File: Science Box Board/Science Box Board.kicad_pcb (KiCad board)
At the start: 2 copper layers, 124.5 x 81.3 mm, 43 parts, among them U1 Molex_SL-2, U10 LB1930MC, U11 Molex_SL-10, U12 Molex_SL_2, U13 Molex_SL_5, U2 Molex_SL-2, U3 5V OKI, U4 OPA320, U5 OPA320, U6 5V OKI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

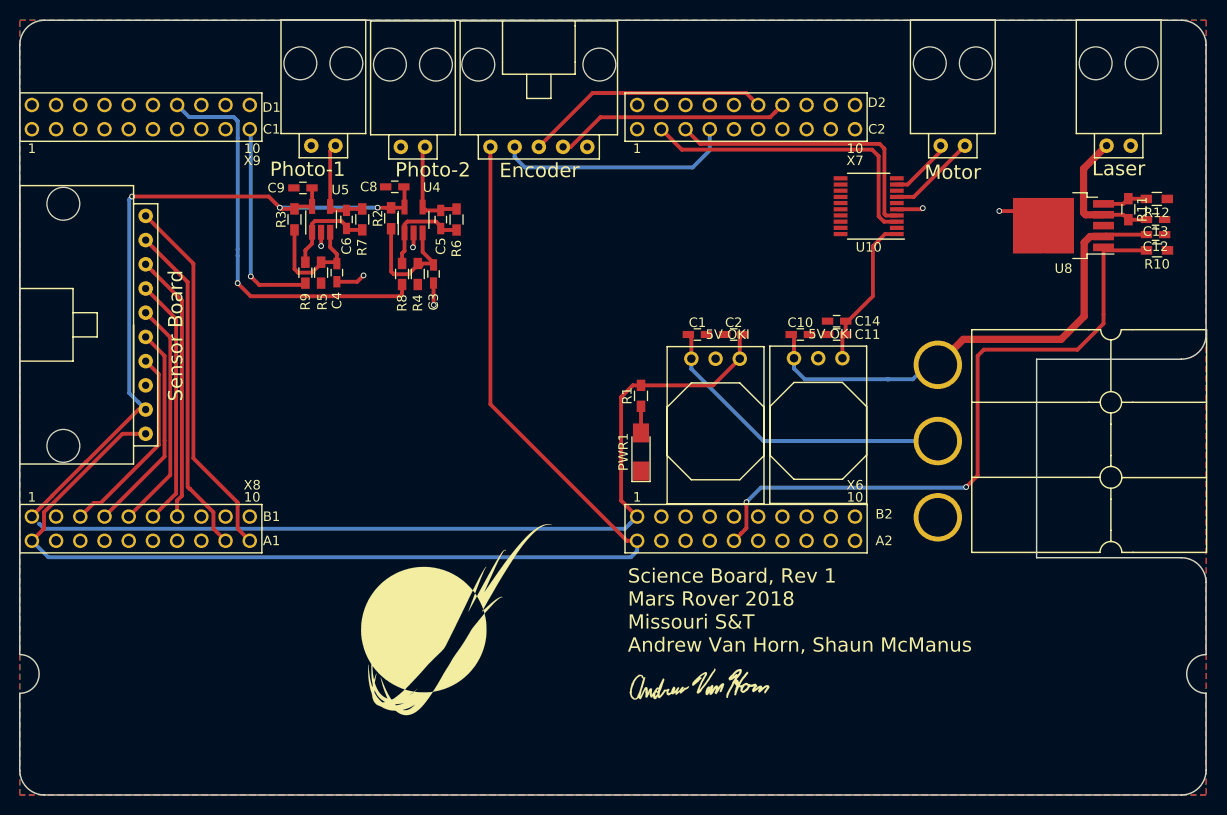
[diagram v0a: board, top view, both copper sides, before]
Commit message: Finalized board and generated gerbs
Changed name of board from "Science Signals Booster" to "Science Box Board". Board Review for Rev 1, generated Gerbs
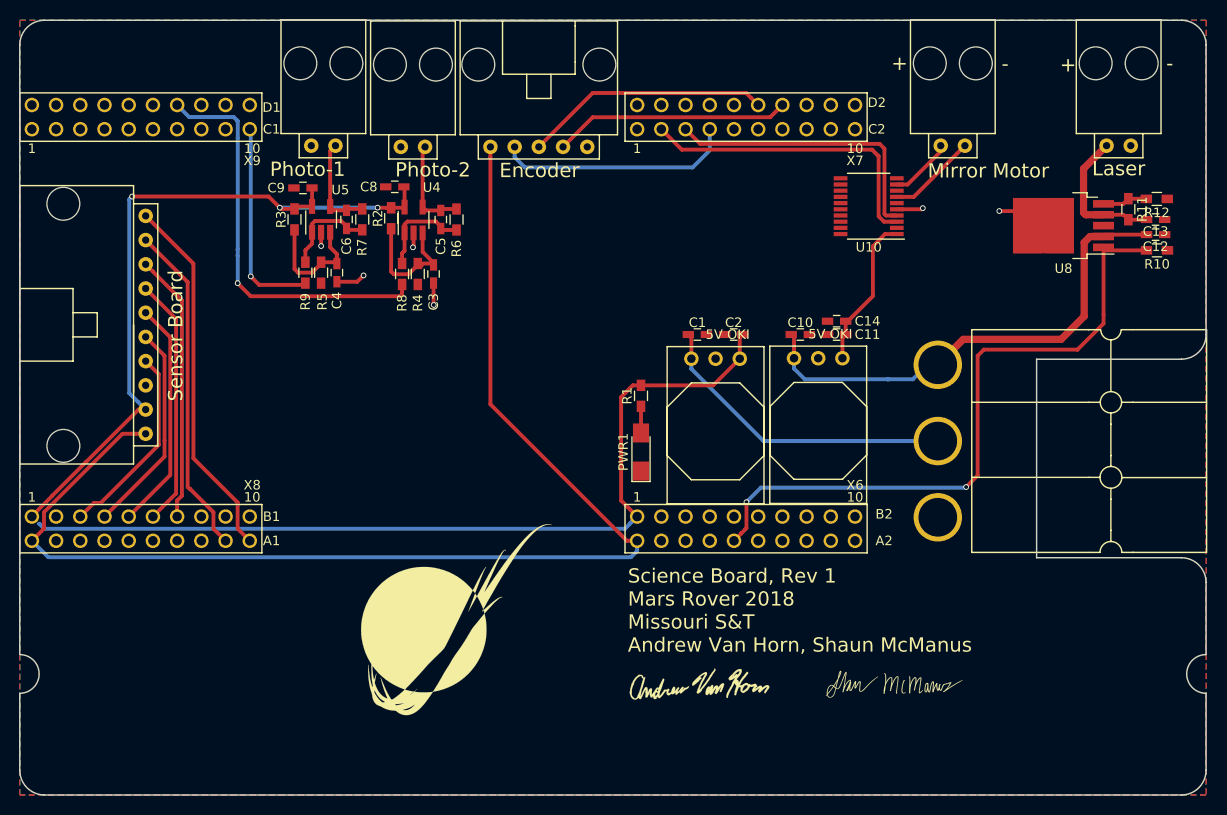
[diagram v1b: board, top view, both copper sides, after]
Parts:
- added G***: LOGO, MRDT_Silkscreens:Shaun_McManus_Sig_15mm, F.Cu at (209.8, 140.9)
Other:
- board text added: "+"
- board text added: "-"
- board text added: "Mirror Motor"
- board text removed: "Motor"

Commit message: Generated Final Gerbs
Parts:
- U10: footprint Housings_SSOP:TSSOP-20_4.4x6.5mm_Pitch0.65mm -> MRDT_ICs:SOIC_10NB_2
- moved U10 3.03 mm to (206.8, 87.9), turned to 270 degrees
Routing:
- net ACT-5V: track 16.2 -> 21.2 mm
- net GND: track 14.1 -> 11.3 mm, vias 6 -> 5
- net MOTOR_IN1: track 32.4 -> 30.5 mm
- net Net-(U10-Pad7): track 9.37 -> 10.3 mm
- net MOTOR_IN2: track 29.9 -> 30.5 mm

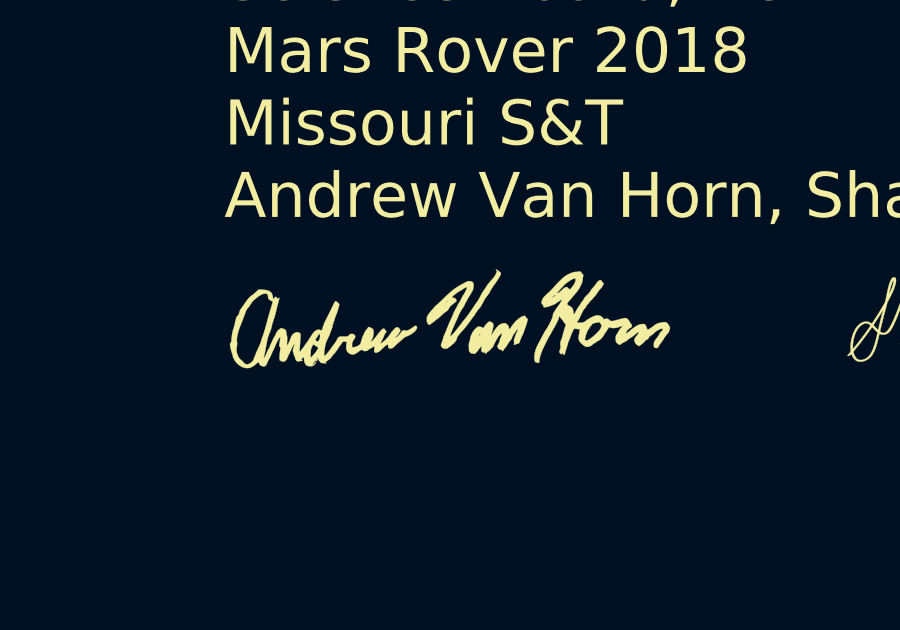
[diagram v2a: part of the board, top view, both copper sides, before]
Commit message: Modified board layout
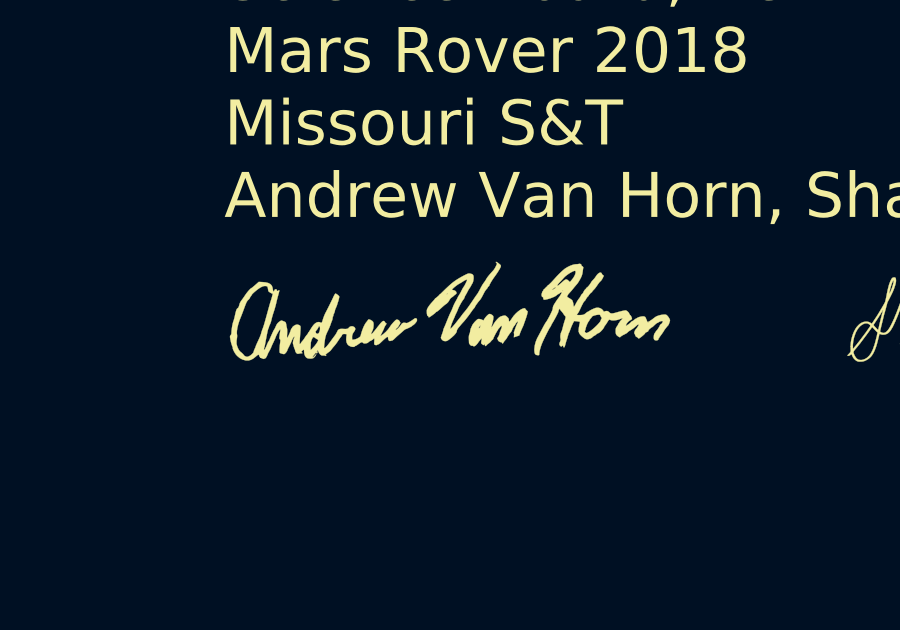
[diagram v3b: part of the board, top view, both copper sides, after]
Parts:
- moved G*** 0.25 mm to (189.2, 140.7)
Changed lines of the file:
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@@
     (links 102)
     (no_connects 2)
-    (area 117.933399 71.349799 242.543401 152.779801)
+    (area 117.5584 71.098999 242.798201 152.979801)
     (thickness 1.6)
     (drawings 29)
@@
   )
   (setup
-    (last_trace_width 0.4064)
+    (last_trace_width 0.25)
     (user_trace_width 0.254)
     (user_trace_width 0.4064)
@@
   )
   (module MRDT_Silkscreens:Andrew_Van_Horn_Sig_15mm (layer F.Cu)
-    (at 189.23 140.97)
+    (at 189.23 140.716)
     (fp_text reference G*** (at 0 2.413) (layer F.Fab) hide
       (effects (font (size 0.5 0.5) (thickness 0.125)))

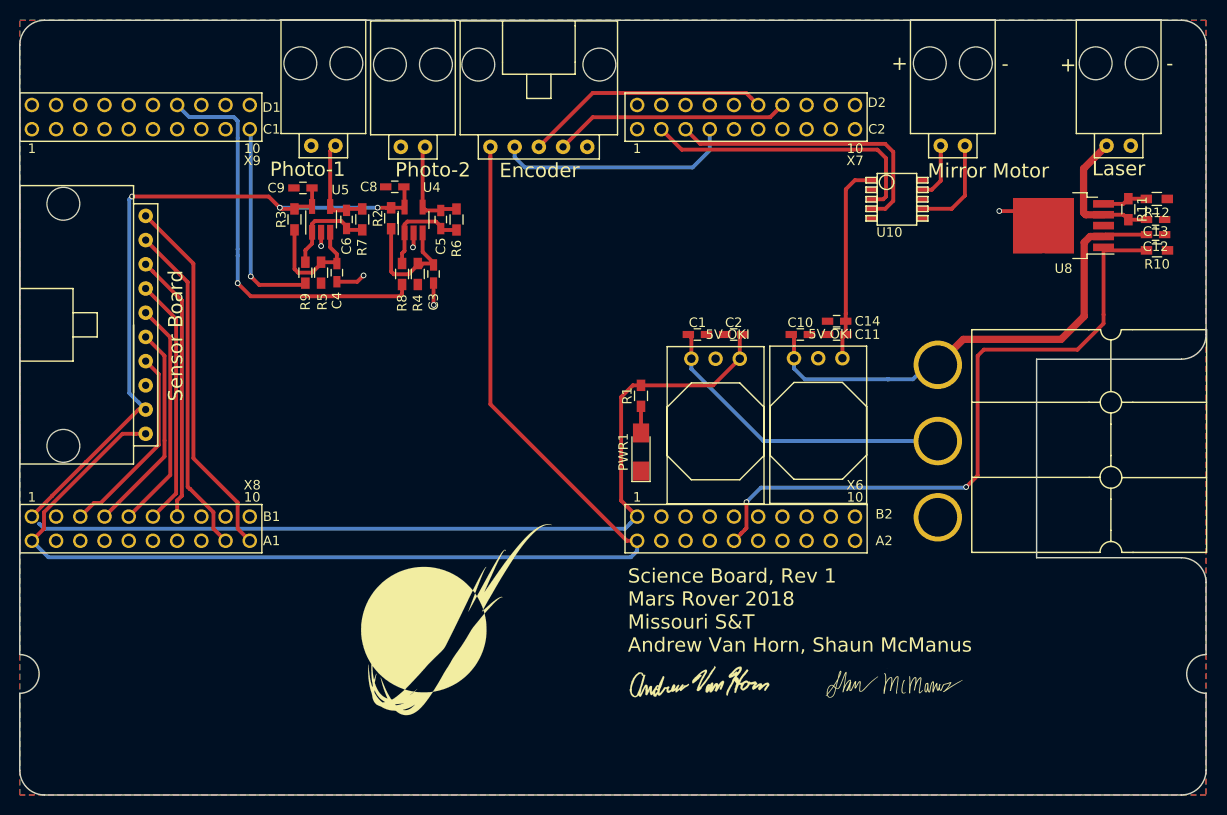
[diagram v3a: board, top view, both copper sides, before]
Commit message: Added new Ba00dwop footrpint and switched SL2 to SL3 for Photodiode
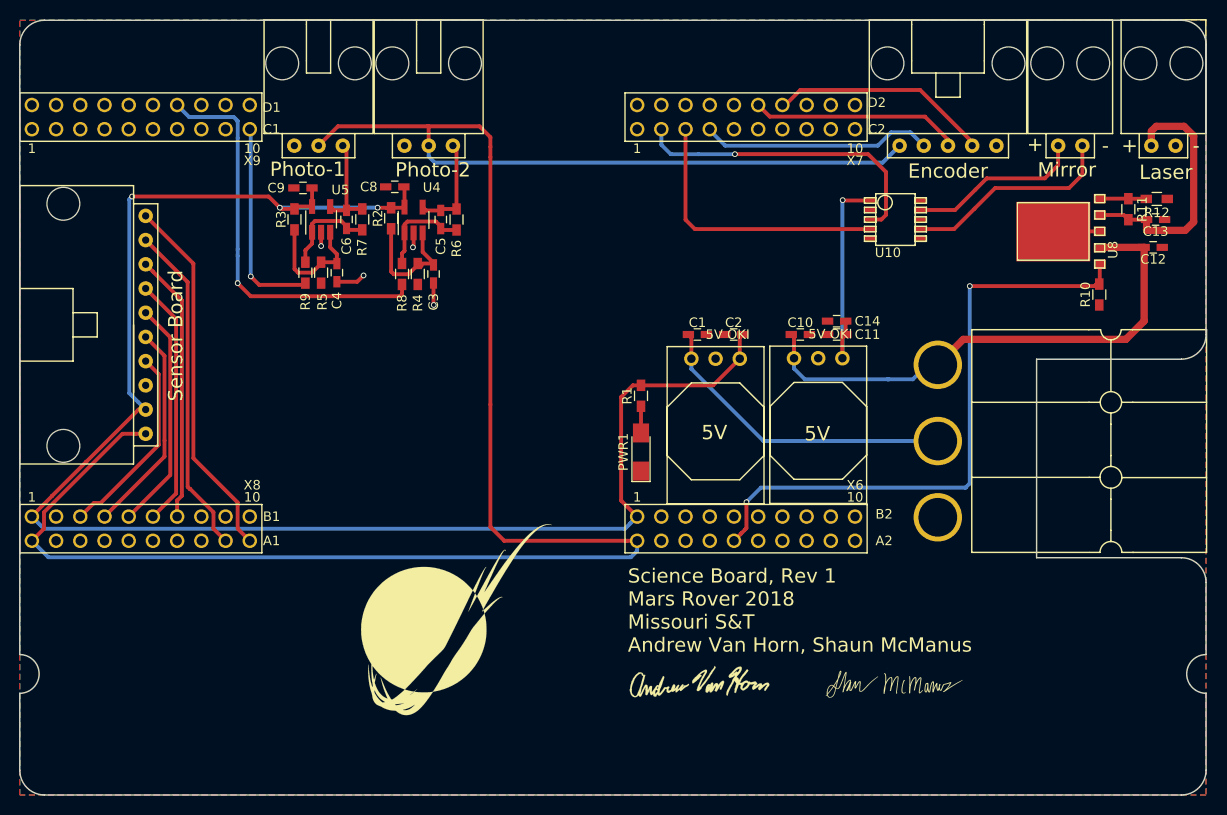
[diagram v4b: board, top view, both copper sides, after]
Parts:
- U1, U2: footprint MRDT_Connectors:MOLEX_SL_2_Horizontal -> MRDT_Connectors:MOLEX_SL_3_Horizontal
- U8: footprint TO_SOT_Packages_SMD:TO-252-5_TabPin3 -> MRDT_ICs:HRP5
- moved U13 42.9 mm to (215.4, 84.6)
- moved U9 12.3 mm to (228.2, 84.6)
- moved R10 7.62 mm to (231.3, 100.2), turned to 90 degrees
- moved U8 6.21 mm to (231.8, 97.4), turned to 90 degrees
- moved U12 4.70 mm to (238.0, 84.6)
- moved U10 2.13 mm to (206.6, 90.0)
- moved U1 1.66 mm to (160.9, 84.6)
- moved C12 1.36 mm to (236.9, 95.2)
- moved U2 0.51 mm to (149.4, 84.6)
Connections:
- U1 pad 2: Net-(C5-Pad2) -> +3V3
- U2 pad 2: Net-(C6-Pad2) -> +3V3
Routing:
- net +3V3: track 131.5 -> 213.0 mm
- net Net-(C13-Pad2): track 14.9 -> 27.2 mm
- net Net-(U10-Pad7): track 10.3 -> 22.4 mm
- net Net-(U10-Pad9): track 6.61 -> 18.4 mm
- net LASER-CTRL_AIN_7: track 69.8 -> 65.4 mm
- net ACT-12V: track 52.1 -> 56.1 mm
- net magINCn: track 25.9 -> 22.1 mm
- net ACT-5V: track 21.2 -> 23.8 mm, vias 0 -> 1
- net MOTOR_IN1: track 30.5 -> 32.8 mm, vias 0 -> 1
- net GND: track 11.3 -> 13.3 mm, vias 5 -> 4
- net magDECn: track 24.8 -> 23.2 mm
- net MOTOR_IN2: track 30.5 -> 29.3 mm
- net LOGIC-5V: track 171.2 -> 172.3 mm
- net LINEAR_ENCODER: track 25.0 -> 24.4 mm
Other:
- board text added: "5V"
- board text added: "Mirror"
- board text removed: "Mirror Motor"
